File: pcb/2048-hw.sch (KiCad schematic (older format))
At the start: 98 parts, among them J1 UJC-HP-3-SMT-TR, J2 Battery, J3 SWD, SW1 SW_SPDT, SW2 PUSH_A, SW3 PUSH_B, U1 STM32F303K8Tx, U2 MCP73831-2-OT, U3 AP2210N-3.3TRG1, U4 PSP_1000_JSTK, U5 LMV339, Y1 NX8045GB-8MHZ

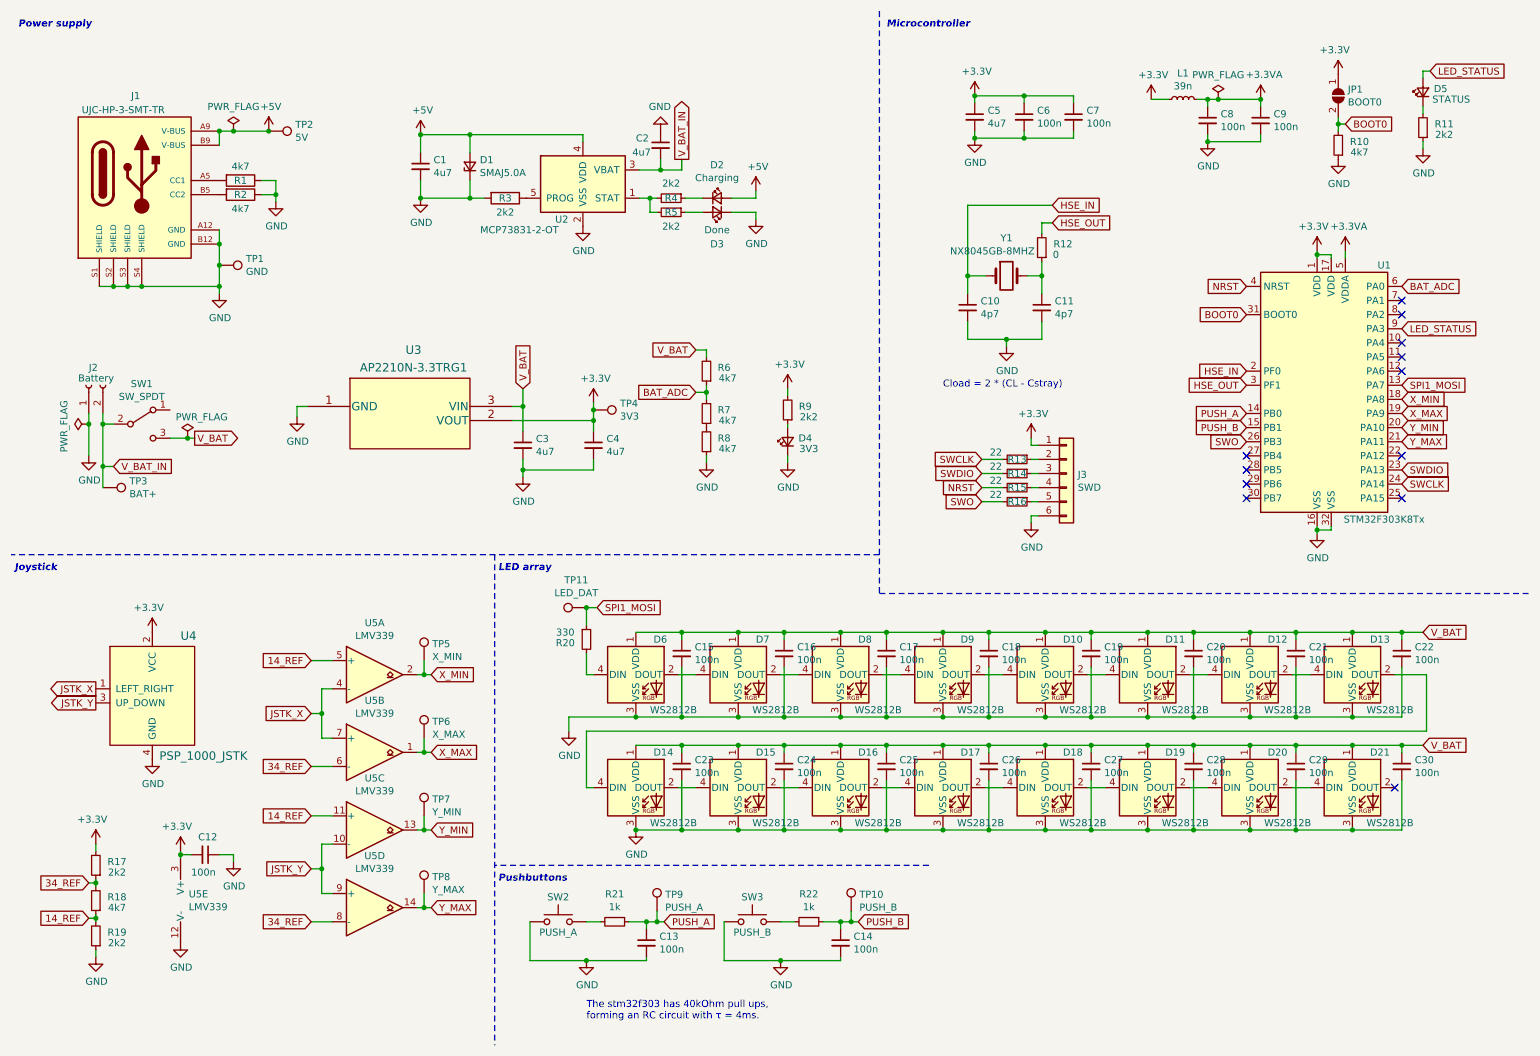
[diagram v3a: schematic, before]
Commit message: Combine libraries into single library
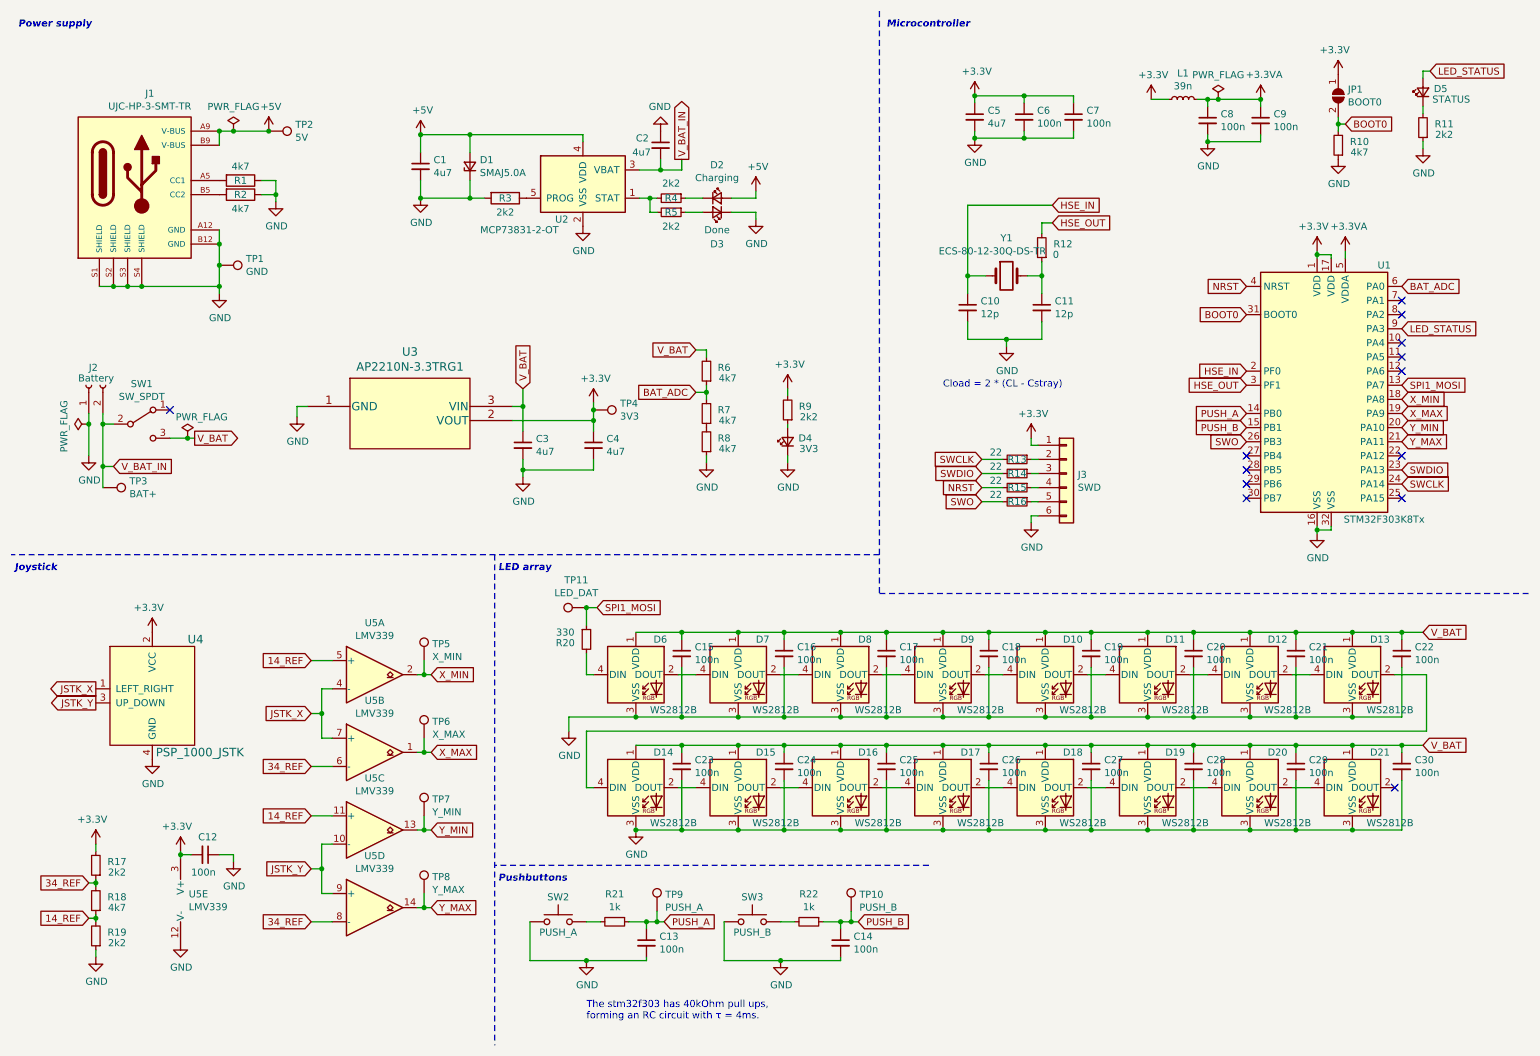
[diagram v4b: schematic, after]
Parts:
- removed J1: UJC-HP-3-SMT-TR, CUI_UJC-HP-3-SMT-TR:CUI_UJC-HP-3-SMT-TR, symbol UJC-HP-3-SMT-TR:UJC-HP-3-SMT-TR
- removed U3: AP2210N-3.3TRG1, Package_TO_SOT_SMD:SOT-23, symbol ap2210:AP2210N-3.3TRG1
- removed U4: PSP_1000_JSTK, psp1000:JOYSTICK-PSP1000, symbol psp_1000_jstk-hackpackv4:PSP_1000_JSTK-HackPackv4-rescue
- added J1: UJC-HP-3-SMT-TR, 2048-hw:CUI_UJC-HP-3-SMT-TR, symbol 2048-hw:UJC-HP-3-SMT-TR
- added U3: AP2210N-3.3TRG1, 2048-hw:AP2210N-3.3TRG1, symbol 2048-hw:AP2210N-3.3TRG1
- added U4: PSP_1000_JSTK, 2048-hw:JOYSTICK-PSP1000, symbol 2048-hw:PSP_1000_JSTK-HackPackv4
- C10, C11: value 4p7 -> 12p
- J2: footprint Battery:BatteryHolder_Keystone_2460_1xAA -> 2048-hw:BatteryHolder_Keystone_2460_1xAA
- SW1: footprint OS102011MS2QN1:SW_OS102011MS2QN1 -> 2048-hw:SW_OS102011MS2QN1
- Y1: value NX8045GB-8MHZ -> ECS-80-12-30Q-DS-TR; footprint (none) -> 2048-hw:XTAL_ECS-80-18-30-JGN-TR
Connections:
- net +3V3: now also U3.2 (VOUT), U4.2 (VCC)
- net +5V: now also J1.A9 (V-BUS), J1.B9 (V-BUS)
- net GND: now also J1.A12 (GND), J1.B12 (GND), J1.S1 (SHIELD), J1.S2 (SHIELD), J1.S3 (SHIELD), J1.S4 (SHIELD), U3.1 (GND), U4.4 (GND)
- net JSTK_X: now also U4.1 (LEFT_RIGHT)
- net JSTK_Y: now also U4.3 (UP_DOWN)
- net V_BAT: now also U3.3 (VIN)
- net at R1.2: now also J1.A5 (CC1)
- net at R2.2: now also J1.B5 (CC2)
- no-connect marks 12 -> 13
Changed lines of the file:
@@
 F 0 "J2" V 1150 3125 50  0000 R CNN
 F 1 "Battery" V 1075 3200 50  0000 R CNN
-F 2 "Battery:BatteryHolder_Keystone_2460_1xAA" H 1025 3125 50  0001 C CNN
+F 2 "2048-hw:BatteryHolder_Keystone_2460_1xAA" H 1025 3125 50  0001 C CNN
 F 3 "~" H 1025 3125 50  0001 C CNN
 	1    1025 3125
 	0    -1   -1   0
-$EndComp
-$Comp
-L psp_1000_jstk-hackpackv4:PSP_1000_JSTK-HackPackv4-rescue U4
-U 1 1 5FEF3AB3
-P 1475 5325
-F 0 "U4" H 1675 5750 60  0000 L CNN
-F 1 "PSP_1000_JSTK" H 1525 4900 60  0000 L CNN
-F 2 "psp1000:JOYSTICK-PSP1000" H 2775 4625 60  0001 C CNN
-F 3 "https://media.digikey.com/pdf/Data%20Sheets/Sparkfun%20PDFs/COM-09426_Web.pdf" H 2775 4625 60  0001 C CNN
-	1    1475 5325
-	1    0    0    -1
 $EndComp
 $Comp
@@
 P 7775 2575
 F 0 "C11" H 7867 2621 50  0000 L CNN
-F 1 "4p7" H 7867 2530 50  0000 L CNN
+F 1 "12p" H 7867 2530 50  0000 L CNN
 F 2 "Capacitor_SMD:C_0603_1608Metric_Pad1.08x0.95mm_HandSolder" H 7775 2575 50  0001 C CNN
 F 3 "~" H 7775 2575 50  0001 C CNN
@@
 P 7250 2575
 F 0 "C10" H 7342 2621 50  0000 L CNN
-F 1 "4p7" H 7342 2530 50  0000 L CNN
+F 1 "12p" H 7342 2530 50  0000 L CNN
 F 2 "Capacitor_SMD:C_0603_1608Metric_Pad1.08x0.95mm_HandSolder" H 7250 2575 50  0001 C CNN
 F 3 "~" H 7250 2575 50  0001 C CNN
 	1    7250 2575
-	1    0    0    -1
-$EndComp
-$Comp
-L Device:Crystal Y1
-U 1 1 5FFA9BCF
-P 7525 2350
-F 0 "Y1" H 7525 2618 50  0000 C CNN
-F 1 "NX8045GB-8MHZ " H 7425 2525 50  0000 C CNN
-F 2 "" H 7525 2350 50  0001 C CNN
-F 3 "~" H 7525 2350 50  0001 C CNN
-	1    7525 2350
 	1    0    0    -1
 $EndComp
@@
 $EndComp
 $Comp
-L ap2210:AP2210N-3.3TRG1 U3
-U 1 1 5FEF5741
-P 2575 3275
-F 0 "U3" H 3325 3675 60  0000 C CNN
-F 1 "AP2210N-3.3TRG1" H 3325 3550 60  0000 C CNN
-F 2 "Package_TO_SOT_SMD:SOT-23" H 3375 3515 60  0001 C CNN
-F 3 "" H 2575 3275 60  0000 C CNN
-	1    2575 3275
-	1    0    0    -1
-$EndComp
-$Comp
 L power:GND #PWR0114
 U 1 1 5FEF6103
@@
 NoConn ~ 10325 2925
 NoConn ~ 10325 3025
-$Comp
-L UJC-HP-3-SMT-TR:UJC-HP-3-SMT-TR J1
-U 1 1 6048B896
-P 1350 1725
-F 0 "J1" H 1325 2375 50  0000 L CNN
-F 1 "UJC-HP-3-SMT-TR" H 975 2275 50  0000 L CNN
-F 2 "CUI_UJC-HP-3-SMT-TR:CUI_UJC-HP-3-SMT-TR" H 1350 1725 50  0001 L BNN
-F 3 "" H 1350 1725 50  0001 L BNN
-F 4 "1.0" H 1350 1725 50  0001 L BNN "PARTREV"
-F 5 "CUI Devices" H 1350 1725 50  0001 L BNN "MANUFACTURER"
-F 6 "3.16mm" H 1350 1725 50  0001 L BNN "MAXIMUM_PACKAGE_HEIGHT"
-F 7 "Manufacturer Recommendations" H 1350 1725 50  0001 L BNN "STANDARD"
-	1    1350 1725
-	1    0    0    -1
-$EndComp
-Wire Wire Line
-	1100 2425 1200 2425
-Connection ~ 1200 2425
-Wire Wire Line
-	1200 2425 1300 2425
-Connection ~ 1300 2425
-Wire Wire Line
-	1300 2425 1400 2425
-Connection ~ 1400 2425
-Wire Wire Line
-	1950 2025 1950 2125
-Wire Wire Line
-	1400 2425 1950 2425
-Connection ~ 1950 2125
-Wire Wire Line
-	1950 2125 1950 2275
 Connection ~ 1950 2425
 Connection ~ 1950 2275
@@
 Wire Wire Line
 	1950 1325 2050 1325
-Connection ~ 1950 1325
 Connection ~ 2050 1325
 Wire Wire Line
@@
 F 0 "SW1" H 1400 3685 50  0000 C CNN
 F 1 "SW_SPDT" H 1400 3594 50  0000 C CNN
-F 2 "OS102011MS2QN1:SW_OS102011MS2QN1" H 1400 3400 50  0001 C CNN
+F 2 "2048-hw:SW_OS102011MS2QN1" H 1400 3400 50  0001 C CNN
 F 3 "~" H 1400 3400 50  0001 C CNN
 	1    1400 3400
@@
 	1    0    0    -1
 $EndComp
+$Comp
+L 2048-hw:PSP_1000_JSTK-HackPackv4 U4
+U 1 1 5FF9243A
+P 1475 5325
+F 0 "U4" H 1725 5725 60  0000 L CNN
+F 1 "PSP_1000_JSTK" H 1500 4925 60  0000 L CNN
+F 2 "2048-hw:JOYSTICK-PSP1000" H 2775 4625 60  0001 C CNN
+F 3 "" H 2775 4625 60  0001 C CNN
+	1    1475 5325
+	1    0    0    -1
+$EndComp
+$Comp
+L 2048-hw:UJC-HP-3-SMT-TR J1
+U 1 1 5FF752B0
+P 1350 1725
+F 0 "J1" H 1457 2392 50  0000 C CNN
+F 1 "UJC-HP-3-SMT-TR" H 1457 2301 50  0000 C CNN
+F 2 "2048-hw:CUI_UJC-HP-3-SMT-TR" H 1450 1125 50  0001 L BNN
+F 3 "" H 1250 1625 50  0001 L BNN
+	1    1350 1725
+	1    0    0    -1
+$EndComp
+Wire Wire Line
+	1950 2125 1950 2275
+Connection ~ 1950 1325
+Wire Wire Line
+	1400 2425 1950 2425
+$Comp
+L 2048-hw:AP2210N-3.3TRG1 U3
+U 1 1 5FF78AFF
+P 2575 3275
+F 0 "U3" H 3300 3662 60  0000 C CNN
+F 1 "AP2210N-3.3TRG1" H 3300 3556 60  0000 C CNN
+F 2 "2048-hw:AP2210N-3.3TRG1" H 3375 3515 60  0001 C CNN
+F 3 "" H 2575 3275 60  0000 C CNN
+	1    2575 3275
+	1    0    0    -1
+$EndComp
+$Comp
+L Device:Crystal Y1
+U 1 1 5FFA9BCF
+P 7525 2350
+F 0 "Y1" H 7525 2618 50  0000 C CNN
+F 1 " ECS-80-12-30Q-DS-TR" H 7425 2525 50  0000 C CNN
+F 2 "2048-hw:XTAL_ECS-80-18-30-JGN-TR" H 7525 2350 50  0001 C CNN
+F 3 "~" H 7525 2350 50  0001 C CNN
+	1    7525 2350
+	1    0    0    -1
+$EndComp
+Wire Wire Line
+	1400 2425 1300 2425
+Connection ~ 1400 2425
+Connection ~ 1200 2425
+Wire Wire Line
+	1200 2425 1100 2425
+Connection ~ 1300 2425
+Wire Wire Line
+	1300 2425 1200 2425
+Wire Wire Line
+	1950 2025 1950 2125
+Connection ~ 1950 2125
+NoConn ~ 1600 3300
 $EndSCHEMATC

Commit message: Group components in layout
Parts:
- TP1, TP10, TP11, TP2, TP3, TP4, TP5, TP6, TP7, TP8, TP9: footprint TestPoint:TestPoint_THTPad_D2.0mm_Drill1.0mm -> TestPoint:TestPoint_THTPad_D1.5mm_Drill0.7mm
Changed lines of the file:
@@
 F 0 "TP2" V 2254 1513 50  0000 L CNN
 F 1 "5V" V 2345 1513 50  0000 L CNN
-F 2 "TestPoint:TestPoint_THTPad_D2.0mm_Drill1.0mm" H 2500 1325 50  0001 C CNN
+F 2 "TestPoint:TestPoint_THTPad_D1.5mm_Drill0.7mm" H 2500 1325 50  0001 C CNN
 F 3 "~" H 2500 1325 50  0001 C CNN
 	1    2300 1325
@@
 F 0 "TP3" V 1079 4038 50  0000 L CNN
 F 1 "BAT+" V 1170 4038 50  0000 L CNN
-F 2 "TestPoint:TestPoint_THTPad_D2.0mm_Drill1.0mm" H 1325 3850 50  0001 C CNN
+F 2 "TestPoint:TestPoint_THTPad_D1.5mm_Drill0.7mm" H 1325 3850 50  0001 C CNN
 F 3 "~" H 1325 3850 50  0001 C CNN
 	1    1125 3850
@@
 F 0 "TP1" V 1904 2463 50  0000 L CNN
 F 1 "GND" V 1995 2463 50  0000 L CNN
-F 2 "TestPoint:TestPoint_THTPad_D2.0mm_Drill1.0mm" H 2150 2275 50  0001 C CNN
+F 2 "TestPoint:TestPoint_THTPad_D1.5mm_Drill0.7mm" H 2150 2275 50  0001 C CNN
 F 3 "~" H 2150 2275 50  0001 C CNN
 	1    1950 2275
@@
 F 0 "TP4" V 4554 3488 50  0000 L CNN
 F 1 "3V3" V 4645 3488 50  0000 L CNN
-F 2 "TestPoint:TestPoint_THTPad_D2.0mm_Drill1.0mm" H 4800 3300 50  0001 C CNN
+F 2 "TestPoint:TestPoint_THTPad_D1.5mm_Drill0.7mm" H 4800 3300 50  0001 C CNN
 F 3 "~" H 4800 3300 50  0001 C CNN
 	1    4600 3300
@@
 F 0 "TP11" V 4745 4772 50  0000 C CNN
 F 1 "LED_DAT" V 4654 4772 50  0000 C CNN
-F 2 "TestPoint:TestPoint_THTPad_D2.0mm_Drill1.0mm" H 4750 4700 50  0001 C CNN
+F 2 "TestPoint:TestPoint_THTPad_D1.5mm_Drill0.7mm" H 4750 4700 50  0001 C CNN
 F 3 "~" H 4750 4700 50  0001 C CNN
 	1    4550 4700
@@
 F 0 "TP5" H 3458 5193 50  0000 L CNN
 F 1 "X_MIN" H 3458 5102 50  0000 L CNN
-F 2 "TestPoint:TestPoint_THTPad_D2.0mm_Drill1.0mm" H 3600 5075 50  0001 C CNN
+F 2 "TestPoint:TestPoint_THTPad_D1.5mm_Drill0.7mm" H 3600 5075 50  0001 C CNN
 F 3 "~" H 3600 5075 50  0001 C CNN
 	1    3400 5075
@@
 F 0 "TP6" H 3458 5743 50  0000 L CNN
 F 1 "X_MAX" H 3458 5652 50  0000 L CNN
-F 2 "TestPoint:TestPoint_THTPad_D2.0mm_Drill1.0mm" H 3600 5625 50  0001 C CNN
+F 2 "TestPoint:TestPoint_THTPad_D1.5mm_Drill0.7mm" H 3600 5625 50  0001 C CNN
 F 3 "~" H 3600 5625 50  0001 C CNN
 	1    3400 5625
@@
 F 0 "TP7" H 3458 6293 50  0000 L CNN
 F 1 "Y_MIN" H 3458 6202 50  0000 L CNN
-F 2 "TestPoint:TestPoint_THTPad_D2.0mm_Drill1.0mm" H 3600 6175 50  0001 C CNN
+F 2 "TestPoint:TestPoint_THTPad_D1.5mm_Drill0.7mm" H 3600 6175 50  0001 C CNN
 F 3 "~" H 3600 6175 50  0001 C CNN
 	1    3400 6175
@@
 F 0 "TP8" H 3458 6843 50  0000 L CNN
 F 1 "Y_MAX" H 3458 6752 50  0000 L CNN
-F 2 "TestPoint:TestPoint_THTPad_D2.0mm_Drill1.0mm" H 3600 6725 50  0001 C CNN
+F 2 "TestPoint:TestPoint_THTPad_D1.5mm_Drill0.7mm" H 3600 6725 50  0001 C CNN
 F 3 "~" H 3600 6725 50  0001 C CNN
 	1    3400 6725
@@
 F 0 "TP9" H 5108 6968 50  0000 L CNN
 F 1 "PUSH_A" H 5108 6877 50  0000 L CNN
-F 2 "TestPoint:TestPoint_THTPad_D2.0mm_Drill1.0mm" H 5250 6850 50  0001 C CNN
+F 2 "TestPoint:TestPoint_THTPad_D1.5mm_Drill0.7mm" H 5250 6850 50  0001 C CNN
 F 3 "~" H 5250 6850 50  0001 C CNN
 	1    5050 6850
@@
 F 0 "TP10" H 6483 6968 50  0000 L CNN
 F 1 "PUSH_B" H 6483 6877 50  0000 L CNN
-F 2 "TestPoint:TestPoint_THTPad_D2.0mm_Drill1.0mm" H 6625 6850 50  0001 C CNN
+F 2 "TestPoint:TestPoint_THTPad_D1.5mm_Drill0.7mm" H 6625 6850 50  0001 C CNN
 F 3 "~" H 6625 6850 50  0001 C CNN
 	1    6425 6850

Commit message: Update switches and battery
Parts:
- J2: footprint 2048-hw:BatteryHolder_Keystone_2460_1xAA -> Connector_JST:JST_PH_S2B-PH-K_1x02_P2.00mm_Horizontal
- SW1: footprint 2048-hw:SW_OS102011MS2QN1 -> 2048-hw:E_SWITCH_EG2208A
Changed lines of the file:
@@
 F 0 "J2" V 1150 3125 50  0000 R CNN
 F 1 "Battery" V 1075 3200 50  0000 R CNN
-F 2 "2048-hw:BatteryHolder_Keystone_2460_1xAA" H 1025 3125 50  0001 C CNN
+F 2 "Connector_JST:JST_PH_S2B-PH-K_1x02_P2.00mm_Horizontal" H 1025 3125 50  0001 C CNN
 F 3 "~" H 1025 3125 50  0001 C CNN
 	1    1025 3125
@@
 F 0 "SW1" H 1400 3685 50  0000 C CNN
 F 1 "SW_SPDT" H 1400 3594 50  0000 C CNN
-F 2 "2048-hw:SW_OS102011MS2QN1" H 1400 3400 50  0001 C CNN
+F 2 "2048-hw:E_SWITCH_EG2208A" H 1400 3400 50  0001 C CNN
 F 3 "~" H 1400 3400 50  0001 C CNN
 	1    1400 3400

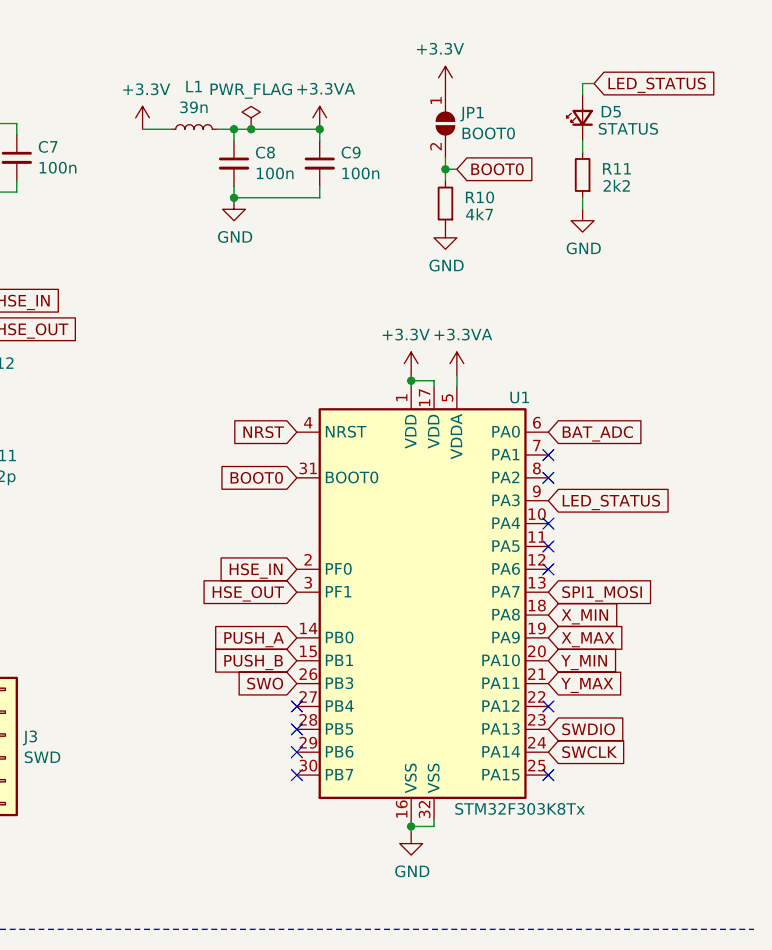
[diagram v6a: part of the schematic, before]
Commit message: Initial layout of components
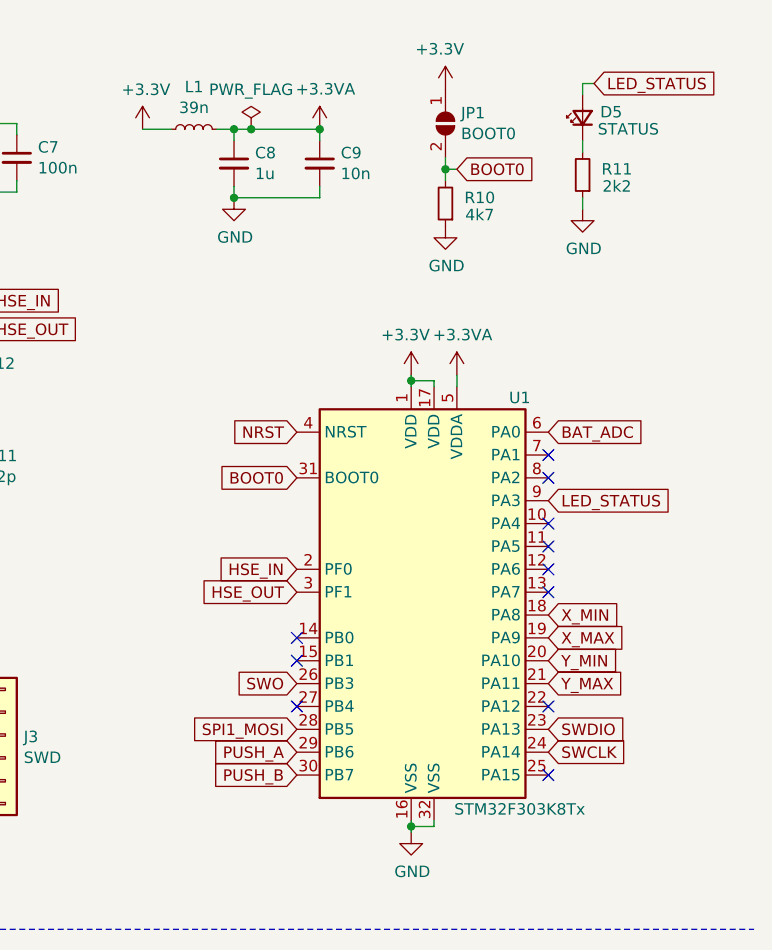
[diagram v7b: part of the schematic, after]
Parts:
- C8: value 100n -> 1u
- C9: value 100n -> 10n
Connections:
- net PUSH_A: now also U1.29 (PB6); no longer U1.14 (PB0)
- net PUSH_B: now also U1.30 (PB7); no longer U1.15 (PB1)
- net SPI1_MOSI: now also U1.28 (PB5); no longer U1.13 (PA7)
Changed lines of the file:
@@
-$Comp
-L Comparator:LMV339 U5
-U 1 1 5FEF95A8
-P 3050 5175
-F 0 "U5" H 3050 5542 50  0000 C CNN
-F 1 "LMV339" H 3050 5451 50  0000 C CNN
-F 2 "Package_SO:SOIC-14_3.9x8.7mm_P1.27mm" H 3000 5275 50  0001 C CNN
-F 3 "https://www.st.com/resource/en/datasheet/lmv331.pdf" H 3100 5375 50  0001 C CNN
-	1    3050 5175
-	1    0    0    -1
-$EndComp
 $Comp
 L Comparator:LMV339 U5
@@
 P 9325 1250
 F 0 "C9" H 9417 1296 50  0000 L CNN
-F 1 "100n" H 9417 1205 50  0000 L CNN
+F 1 "10n" H 9417 1205 50  0000 L CNN
 F 2 "Capacitor_SMD:C_0603_1608Metric_Pad1.08x0.95mm_HandSolder" H 9325 1250 50  0001 C CNN
 F 3 "~" H 9325 1250 50  0001 C CNN
@@
 P 8950 1250
 F 0 "C8" H 9042 1296 50  0000 L CNN
-F 1 "100n" H 9042 1205 50  0000 L CNN
+F 1 "1u" H 9042 1205 50  0000 L CNN
 F 2 "Capacitor_SMD:C_0603_1608Metric_Pad1.08x0.95mm_HandSolder" H 8950 1250 50  0001 C CNN
 F 3 "~" H 8950 1250 50  0001 C CNN
@@
 NoConn ~ 10325 2625
 NoConn ~ 10325 2525
-NoConn ~ 9225 3925
-NoConn ~ 9225 3825
-NoConn ~ 9225 3725
 NoConn ~ 9225 3625
-Text GLabel 10325 2425 2    50   Input ~ 0
-BAT_ADC
 Text GLabel 10325 2725 2    50   Input ~ 0
 LED_STATUS
-Text GLabel 10325 3125 2    50   Input ~ 0
+Text GLabel 9225 3725 0    50   Input ~ 0
 SPI1_MOSI
 Text GLabel 9225 3525 0    50   Input ~ 0
@@
 Wire Wire Line
 	1675 6450 1675 6475
-Text GLabel 9225 3325 0    50   Input ~ 0
+Text GLabel 9225 3825 0    50   Input ~ 0
 PUSH_A
-Text GLabel 9225 3425 0    50   Input ~ 0
+Text GLabel 9225 3925 0    50   Input ~ 0
 PUSH_B
 $Comp
@@
 Connection ~ 1950 2125
 NoConn ~ 1600 3300
+NoConn ~ 10325 3125
+NoConn ~ 9225 3425
+NoConn ~ 9225 3325
+Text GLabel 10325 2425 2    50   Input ~ 0
+BAT_ADC
+$Comp
+L Comparator:LMV339 U5
+U 1 1 5FEF95A8
+P 3050 5175
+F 0 "U5" H 3050 5542 50  0000 C CNN
+F 1 "LMV339" H 3050 5451 50  0000 C CNN
+F 2 "Package_SO:SOIC-14_3.9x8.7mm_P1.27mm" H 3000 5275 50  0001 C CNN
+F 3 "https://www.st.com/resource/en/datasheet/lmv331.pdf" H 3100 5375 50  0001 C CNN
+	1    3050 5175
+	1    0    0    -1
+$EndComp
 $EndSCHEMATC
